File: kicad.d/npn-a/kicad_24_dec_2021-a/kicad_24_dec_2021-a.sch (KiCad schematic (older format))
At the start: 30 parts, among them Q1 2N3904, Q2 2N3906

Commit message: drawing detail clean-up
	modified:   kicad_24_dec_2021-a-cache.lib
	modified:   kicad_24_dec_2021-a.sch

On branch dvlp-aa
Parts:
- removed MES?: unknown, symbol Device:Amperemeter_AC
- removed MES?: 5.116 mA, symbol Device:Amperemeter_AC
- removed MES?: 4.233 mA, symbol Device:Amperemeter_AC
- removed Q?: 2N3906, Package_TO_SOT_THT:TO-92_Inline, symbol Transistor_BJT:2N3906
- removed R?: 47k, symbol Device:R_US
- removed U?: ULN2803A, symbol Transistor_Array:ULN2803A
- removed V?: VPULSE, symbol Simulation_SPICE:VPULSE
- added MES_B-144: -5.09 pA, symbol Device:Amperemeter_AC
- added MES_B-88: 386.217 uA, symbol Device:Amperemeter_AC
- added SW_B-1: SW_SPDT, symbol Switch:SW_SPDT
- MES2: value 92.905 uA -> 386.217 uA
- MES_B-55: renamed from MES?; value 4.326 mA -> 20.554 mA
- MES_B-77: renamed from MES?; value 651 uA -> 20.168 mA
- MES_CC-455: renamed from MES?; value 1.534 mA -> near 1.534 mA
- R_B-1: renamed from R?; value 47k -> 6.8k
- R_B-2: renamed from R?; value 1k -> 100
- gave numbers to parts that had none: 4
- renumbered MES1 to MES_CC-1
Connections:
- net labels added: +5V
- wire segments 28 -> 29
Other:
- note added: "24 Dec 2021 02:31:11z"
- note removed: "24 Dec 2021 01:40:09z"
- moved on the sheet: D1, MES_B-77, Q1_new, R117, R?, R_B-1, R_B-2, V?

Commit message: Circuit updates
	modified:   kicad_24_dec_2021-a.png
	modified:   kicad_24_dec_2021-a.sch
	modified:   kicad_24_dec_2021-a.svg

On branch dvlp-aa
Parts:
- renumbered MES2 to MES_B-33, Q1_new to Q_B-33
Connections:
- wire segments 29 -> 31
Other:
- note added: "24 Dec 2021 03:32:43z"
- note removed: "24 Dec 2021 02:31:11z"
- moved on the sheet: D1, R_B-2
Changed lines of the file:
@@
 U 1 1 61D27D60
 P 6000 3000
-F 0 "MES_B-77" H 5400 3100 50  0000 L CNN
-F 1 "20.168 mA" H 6200 2950 50  0000 L CNN
+F 0 "MES_B-77" H 6200 3050 50  0000 L CNN
+F 1 "20.168 mA" H 6200 2900 50  0000 L CNN
 F 2 "" V 6000 3100 50  0001 C CNN
 F 3 "~" V 6000 3100 50  0001 C CNN
@@
 U 1 1 61CF8DDE
 P 6000 3800
-F 0 "MES_B-55" H 6400 3800 50  0000 C CNN
-F 1 "20.554 mA" H 5847 3800 50  0000 R CNN
+F 0 "MES_B-55" H 6400 3850 50  0000 C CNN
+F 1 "20.554 mA" H 6600 3700 50  0000 R CNN
 F 2 "" V 6000 3900 50  0001 C CNN
 F 3 "~" V 6000 3900 50  0001 C CNN
 	1    6000 3800
-	-1   0    0    -1
+	1    0    0    -1
 $EndComp
 $Comp
@@
 	9750 1800 9750 1650
 $Comp
-L Transistor_BJT:2N3904 Q1_new
+L Transistor_BJT:2N3904 Q_B-33
 U 1 1 61C80D14
 P 5900 3400
-F 0 "Q1_new" H 6090 3446 50  0000 L CNN
-F 1 "2N3904" H 6090 3355 50  0000 L CNN
+F 0 "Q_B-33" H 6150 3450 50  0000 L CNN
+F 1 "2N3904" H 6150 3300 50  0000 L CNN
 F 2 "Package_TO_SOT_THT:TO-92_Inline" H 6100 3325 50  0001 L CIN
 F 3 "https://www.onsemi.com/pub/Collateral/2N3903-D.PDF" H 5900 3400 50  0001 L CNN
@@
 L Device:LED D1
 U 1 1 61C80D07
-P 6000 2650
-F 0 "D1" V 6039 2532 50  0000 R CNN
-F 1 "LED" V 5948 2532 50  0000 R CNN
-F 2 "" H 6000 2650 50  0001 C CNN
-F 3 "~" H 6000 2650 50  0001 C CNN
-	1    6000 2650
+P 6000 2550
+F 0 "D1" V 6039 2432 50  0000 R CNN
+F 1 "LED" V 5948 2432 50  0000 R CNN
+F 2 "" H 6000 2550 50  0001 C CNN
+F 3 "~" H 6000 2550 50  0001 C CNN
+	1    6000 2550
 	0    -1   -1   0
 $EndComp
@@
 L Device:R_US R_B-2
 U 1 1 61C80CE3
-P 6000 2350
-F 0 "R_B-2" H 5750 2450 50  0000 L CNN
-F 1 "100" H 6068 2305 50  0000 L CNN
-F 2 "" V 6040 2340 50  0001 C CNN
-F 3 "~" H 6000 2350 50  0001 C CNN
-	1    6000 2350
+P 6000 2150
+F 0 "R_B-2" H 6100 2250 50  0000 L CNN
+F 1 "100" H 6100 2050 50  0000 L CNN
+F 2 "" V 6040 2140 50  0001 C CNN
+F 3 "~" H 6000 2150 50  0001 C CNN
+	1    6000 2150
 	1    0    0    -1
 $EndComp
@@
  [ https://wiki.analog.com/university/courses/eps/bjt-switch ]
 Text Notes 8200 7650 0    50   ~ 10
-24 Dec 2021  02:31:11z
+24 Dec 2021  03:32:43z
 $Comp
 L power:+5V #PWR?
 U 1 1 61C5C18F
-P 6000 2050
-F 0 "#PWR?" H 6000 1900 50  0001 C CNN
-F 1 "+5V" H 6015 2223 50  0000 C CNN
-F 2 "" H 6000 2050 50  0001 C CNN
-F 3 "" H 6000 2050 50  0001 C CNN
-	1    6000 2050
+P 6000 1850
+F 0 "#PWR?" H 6000 1700 50  0001 C CNN
+F 1 "+5V" H 6015 2023 50  0000 C CNN
+F 2 "" H 6000 1850 50  0001 C CNN
+F 3 "" H 6000 1850 50  0001 C CNN
+	1    6000 1850
 	1    0    0    -1
 $EndComp
@@
 	3700 3500 3700 3550
 $Comp
-L Device:Amperemeter_AC MES2
+L Device:Amperemeter_AC MES_B-33
 U 1 1 61C9332E
 P 5350 3400
-F 0 "MES2" V 5550 3400 50  0000 C CNN
+F 0 "MES_B-33" V 5550 3400 50  0000 C CNN
 F 1 "386.217 uA" V 5150 3400 50  0000 C CNN
 F 2 "" V 5350 3500 50  0001 C CNN
@@
 	5550 3400 5700 3400
 Wire Wire Line
-	6000 2050 6000 2200
+	6000 1850 6000 2000
+Wire Wire Line
+	6000 2700 6000 2800
+Wire Wire Line
+	6000 2300 6000 2400
 $EndSCHEMATC

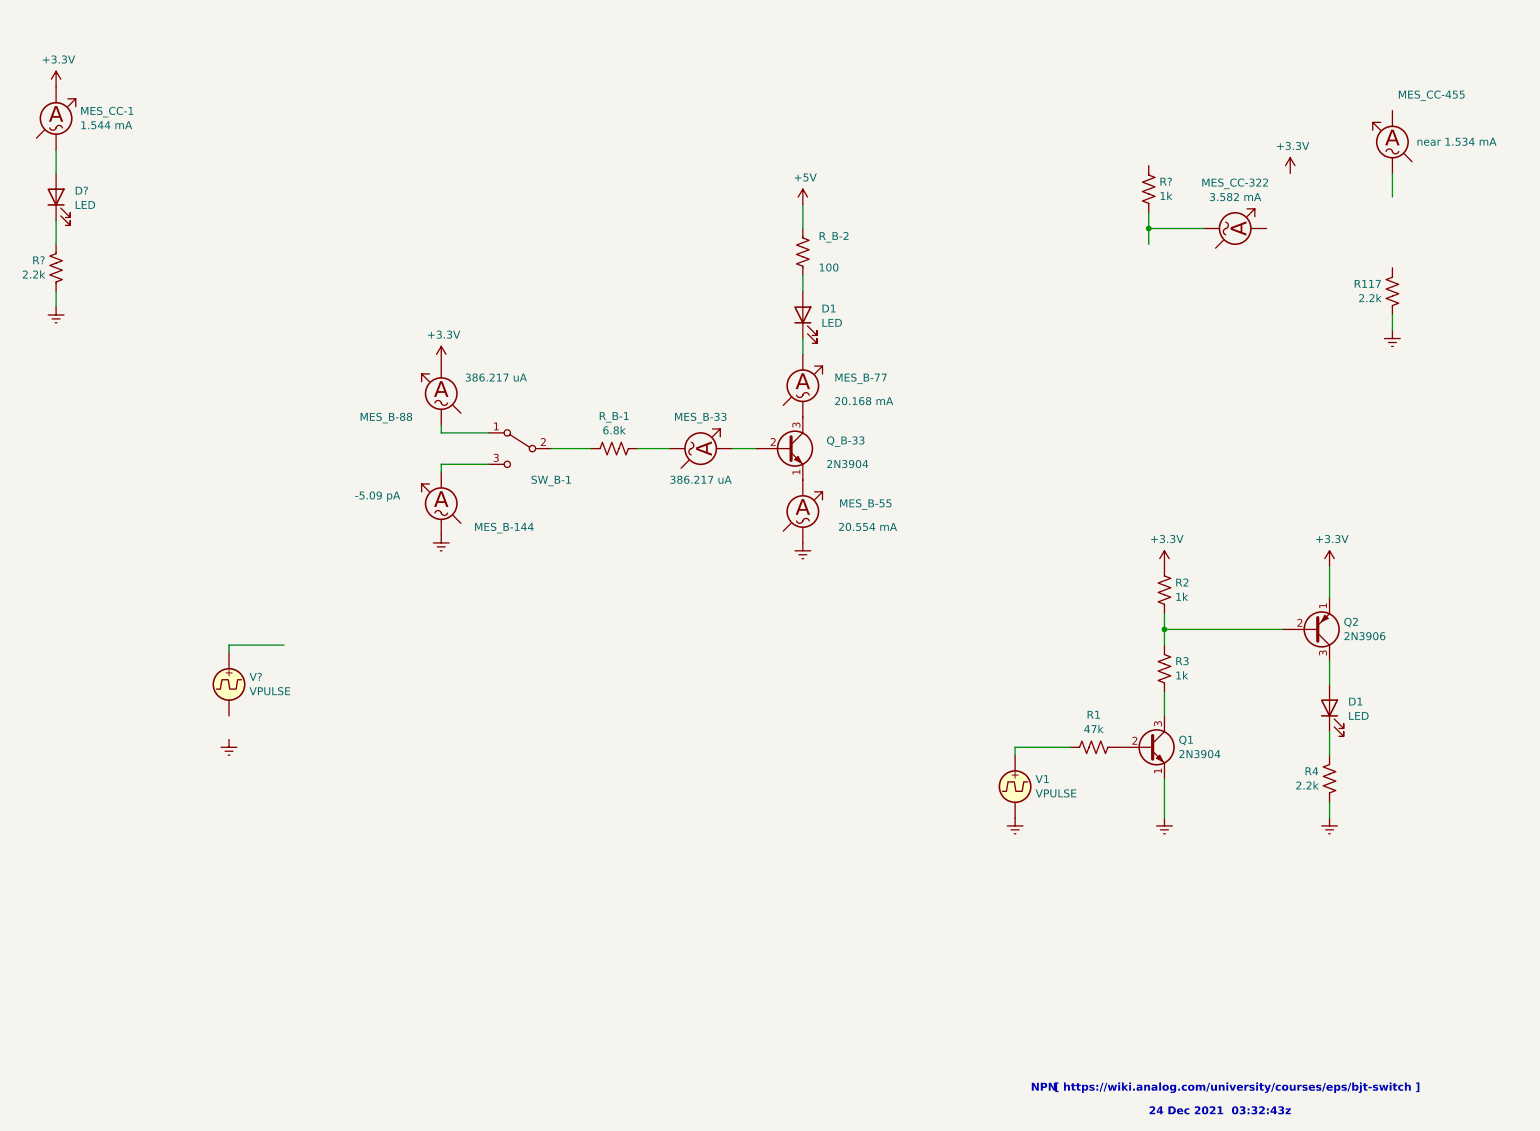
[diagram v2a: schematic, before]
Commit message: Basis of previous commit
	modified:   kicad_24_dec_2021-a-cache.lib
	modified:   kicad_24_dec_2021-a.sch

On branch dvlp-aa
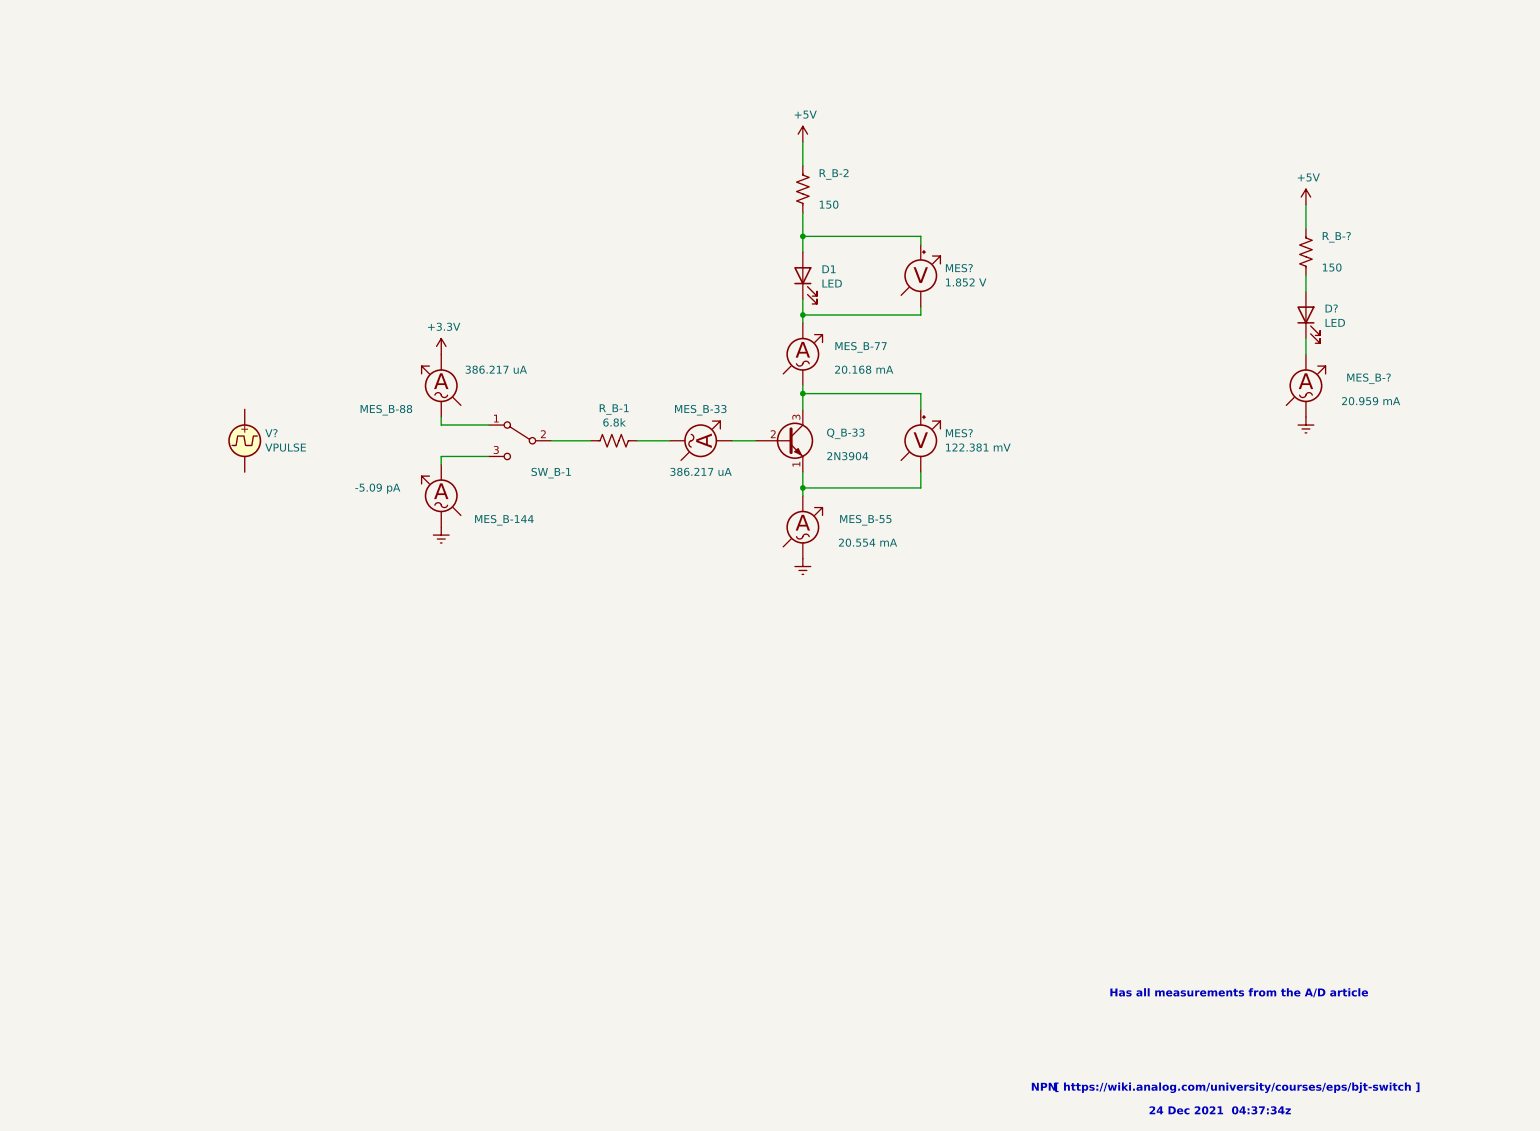
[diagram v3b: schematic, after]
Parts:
- removed D1, D?: LED, symbol Device:LED
- removed MES_CC-1: 1.544 mA, symbol Device:Amperemeter_AC
- removed MES_CC-322: 3.582 mA, symbol Device:Amperemeter_AC
- removed MES_CC-455: near 1.534 mA, symbol Device:Amperemeter_AC
- removed Q1: 2N3904, Package_TO_SOT_THT:TO-92_Inline, symbol Transistor_BJT:2N3904
- removed Q2: 2N3906, Package_TO_SOT_THT:TO-92_Inline, symbol Transistor_BJT:2N3906
- removed R1: 47k, symbol Device:R_US
- removed R117, R4, R?: 2.2k, symbol Device:R_US
- removed R2, R3, R?: 1k, symbol Device:R_US
- removed V1: VPULSE, symbol Simulation_SPICE:VPULSE
- added D?: LED, symbol Device:LED
- added MES?: 122.381 mV, symbol Device:Voltmeter_DC
- added MES?: 1.852 V, symbol Device:Voltmeter_DC
- added MES_B-?: 20.959 mA, symbol Device:Amperemeter_AC
- added R_B-?: 150, symbol Device:R_US
- R_B-2: value 100 -> 150
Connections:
- wire segments 31 -> 27
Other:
- note added: "24 Dec 2021 04:37:34z"
- note added: "Has all measurements from the A/D article"
- note removed: "24 Dec 2021 03:32:43z"
- moved on the sheet: D1, MES_B-144, MES_B-33, MES_B-55, MES_B-77, MES_B-88, Q_B-33, R_B-1, R_B-2, SW_B-1, V?

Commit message: Simplified example added to main drawing.
	modified:   kicad_24_dec_2021-a.png
	modified:   kicad_24_dec_2021-a.sch
	modified:   kicad_24_dec_2021-a.svg

On branch dvlp-aa
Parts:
- removed V?: VPULSE, symbol Simulation_SPICE:VPULSE
- added D?: LED, symbol Device:LED
- added Pulsed_A: 3.3 Vmax, symbol Simulation_SPICE:VPULSE
- added Q_B-?: 2N3904, Package_TO_SOT_THT:TO-92_Inline, symbol Transistor_BJT:2N3904
- added R_B-?: 150, symbol Device:R_US
- added R_B-?: 6.8k, symbol Device:R_US
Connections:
- net +5V: now also R_B-?.1
- net GNDREF: now also Pulsed_A.2, Q_B-?.1 (E)
- new net: Q_B-?.2 (B), R_B-?.2
- new net: D?.1 (K), Q_B-?.3 (C)
- new net: D?.2 (A), R_B-?.2
- new net: Pulsed_A.1, R_B-?.1
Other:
- note added: "24 Dec 2021 04:59:51z"
- note removed: "24 Dec 2021 04:37:34z"
- moved on the sheet: D1, D?, MES?, MES_B-144, MES_B-33, MES_B-55, MES_B-77, MES_B-88, MES_B-?, Q_B-33, R_B-1, R_B-2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
